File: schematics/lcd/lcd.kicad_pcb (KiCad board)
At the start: 2 copper layers, 68.7 x 45.2 mm, 22 parts, among them J1 Conn_01x07_Socket, U1 NHD-C12832A1Z, U2 TLV70033_SOT23-5, U3 TXS0104EDR

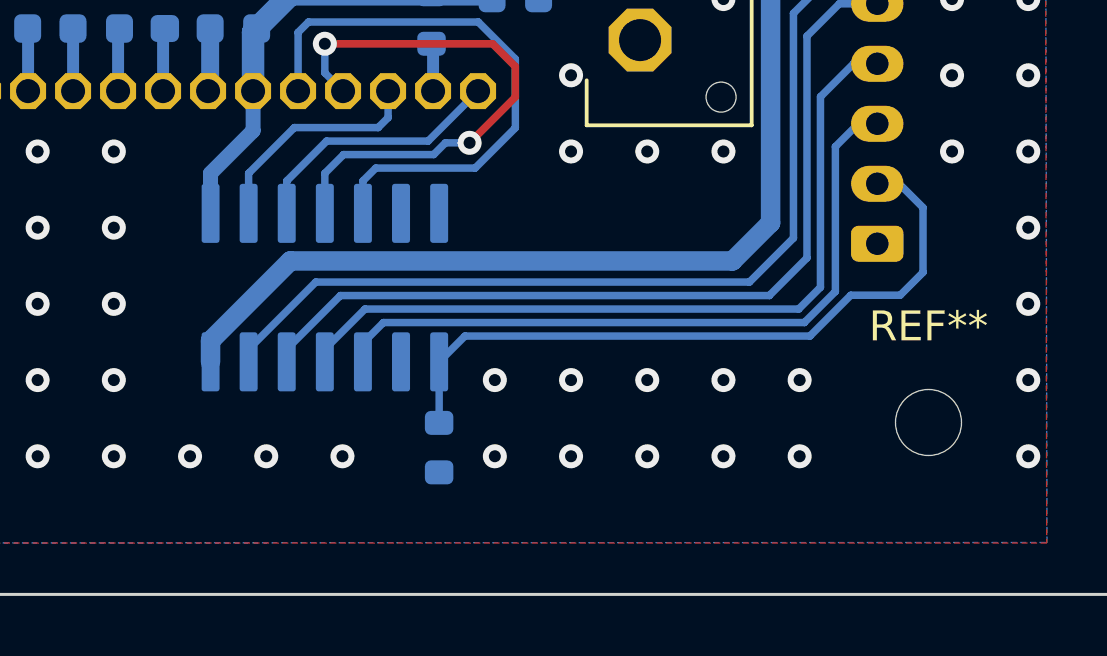
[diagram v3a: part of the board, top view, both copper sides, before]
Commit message: SCH: LCD => removed MB OE connection, now pulled to 3.3, always ON
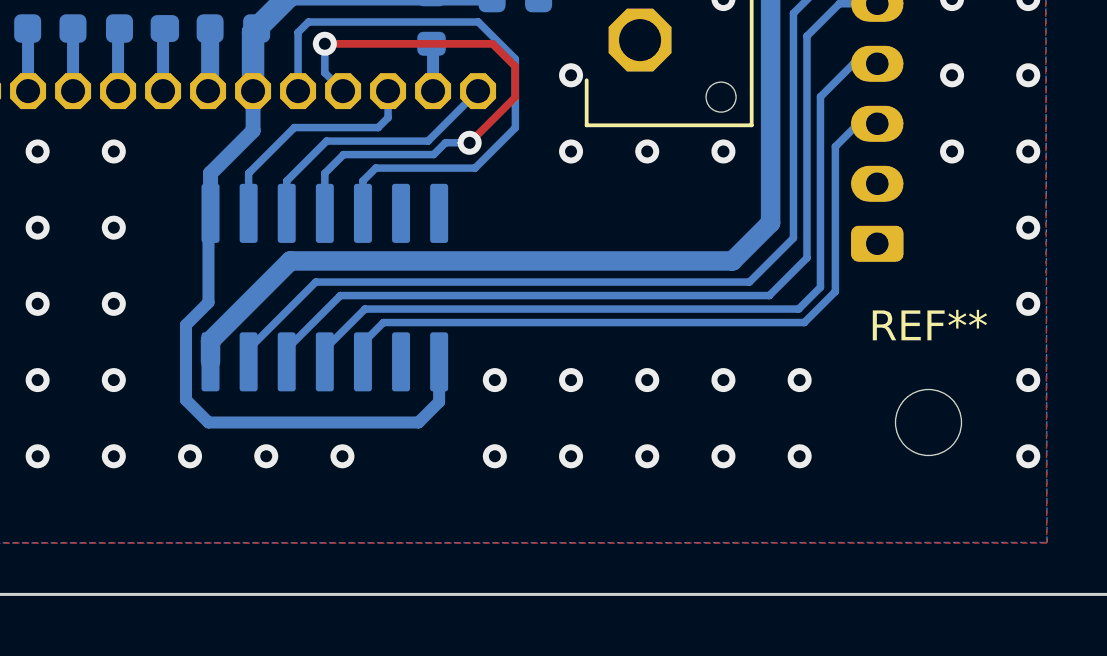
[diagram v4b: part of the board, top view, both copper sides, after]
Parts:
- removed R2: 10K, Resistor_SMD:R_0603_1608Metric
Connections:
- J1 pad 2: /MCU_OE -> GND
- U3 pad 8: /MCU_OE -> +3.3V
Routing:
- net /MCU_OE: track 23.4 -> 0.00 mm
- net +3.3V: track 45.8 -> 62.7 mm
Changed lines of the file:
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@@
   (net 23 "unconnected-(U2-NC-Pad4)")
   (net 24 "VD")
-  (net 25 "/MCU_OE")
   (footprint "MountingHole:MountingHole_2.2mm_M2" (layer "F.Cu")
     (at 67 100)
@@
   (footprint "library:SOIC127P600X175-14N" (layer "B.Cu")
     (at 103.378 95.504 -90)
+    (property "LCSC" "C79342")
     (property "Sheetfile" "lcd.kicad_sch")
     (property "Sheetname" "")
@@
         (effects (font (size 1 1) (thickness 0.15)) (justify mirror))
     )
-    (fp_text value "TXS0104EDR" (at 5.496 2.378) (layer "B.Fab")
+    (fp_text value "TXS0104EDR" (at 8.465 -5.435 90) (layer "B.Fab")
         (effects (font (size 1 1) (thickness 0.15)) (justify mirror))
     )
@@
       (net 2 "GND") (pinfunction "GND") (pintype "power_in"))
     (pad "8" smd roundrect (at 2.475 -3.81 270) (size 1.97 0.6) (layers "B.Cu" "B.Paste" "B.Mask") (roundrect_rratio 0.15)
-      (net 25 "/MCU_OE") (pinfunction "OE") (pintype "input"))
+      (net 3 "+3.3V") (pinfunction "OE") (pintype "input"))
     (pad "9" smd roundrect (at 2.475 -2.54 270) (size 1.97 0.6) (layers "B.Cu" "B.Paste" "B.Mask") (roundrect_rratio 0.15))
     (pad "10" smd roundrect (at 2.475 -1.27 270) (size 1.97 0.6) (layers "B.Cu" "B.Paste" "B.Mask") (roundrect_rratio 0.15)
@@
     )
   )
-  (footprint "Resistor_SMD:R_0603_1608Metric" (layer "B.Cu")
-    (at 107.188 100.838 90)
-    (descr "Resistor SMD 0603 (1608 Metric), square (rectangular) end terminal, IPC_7351 nominal, (Body size source: IPC-SM-782 page 72, https://www.pcb-3d.com/wordpress/wp-content/uploads/ipc-sm-782a_amendment_1_and_2.pdf), generated with kicad-footprint-generator")
-    (tags "resistor")
-    (property "Sheetfile" "lcd.kicad_sch")
-    (property "Sheetname" "")
-    (property "ki_description" "Resistor")
-    (property "ki_keywords" "R res resistor")
-    (property "lcsc" "C25804")
-    (attr smd)
-    (fp_text reference "R2" (at 0 1.43 90) (layer "B.SilkS")
-        (effects (font (size 1 1) (thickness 0.15)) (justify mirror))
-    )
-    (fp_text value "10K" (at 0 -1.43 90) (layer "B.Fab") hide
-        (effects (font (size 1 1) (thickness 0.15)) (justify mirror))
-    )
-    (fp_text user "${REFERENCE}" (at 0 0 90) (layer "B.Fab")
-        (effects (font (size 0.4 0.4) (thickness 0.06)) (justify mirror))
-    )
-    (fp_line (start -0.237258 -0.5225) (end 0.237258 -0.5225)
-      (stroke (width 0.12) (type solid)) (layer "B.SilkS"))
-    (fp_line (start -0.237258 0.5225) (end 0.237258 0.5225)
-      (stroke (width 0.12) (type solid)) (layer "B.SilkS"))
-    (fp_line (start -1.48 -0.73) (end -1.48 0.73)
-      (stroke (width 0.05) (type solid)) (layer "B.CrtYd"))
-    (fp_line (start -1.48 0.73) (end 1.48 0.73)
-      (stroke (width 0.05) (type solid)) (layer "B.CrtYd"))
-    (fp_line (start 1.48 -0.73) (end -1.48 -0.73)
-      (stroke (width 0.05) (type solid)) (layer "B.CrtYd"))
-    (fp_line (start 1.48 0.73) (end 1.48 -0.73)
-      (stroke (width 0.05) (type solid)) (layer "B.CrtYd"))
-    (fp_line (start -0.8 -0.4125) (end -0.8 0.4125)
-      (stroke (width 0.1) (type solid)) (layer "B.Fab"))
-    (fp_line (start -0.8 0.4125) (end 0.8 0.4125)
-      (stroke (width 0.1) (type solid)) (layer "B.Fab"))
-    (fp_line (start 0.8 -0.4125) (end -0.8 -0.4125)
-      (stroke (width 0.1) (type solid)) (layer "B.Fab"))
-    (fp_line (start 0.8 0.4125) (end 0.8 -0.4125)
-      (stroke (width 0.1) (type solid)) (layer "B.Fab"))
-    (pad "1" smd roundrect (at -0.825 0 90) (size 0.8 0.95) (layers "B.Cu" "B.Paste" "B.Mask") (roundrect_rratio 0.25)
-      (net 2 "GND") (pintype "passive"))
-    (pad "2" smd roundrect (at 0.825 0 90) (size 0.8 0.95) (layers "B.Cu" "B.Paste" "B.Mask") (roundrect_rratio 0.25)
-      (net 25 "/MCU_OE") (pintype "passive"))
-    (model "${KICAD6_3DMODEL_DIR}/Resistor_SMD.3dshapes/R_0603_1608Metric.wrl"
-      (offset (xyz 0 0 0))
-      (scale (xyz 1 1 1))
-      (rotate (xyz 0 0 0))
-    )
-  )
   (footprint "Capacitor_SMD:C_0603_1608Metric" (layer "B.Cu")
     (at 98.044 86.093 -90)
@@
       (net 2 "GND") (pinfunction "Pin_1") (pintype "passive"))
     (pad "2" thru_hole oval (at 2 0 90) (size 1.2 1.75) (drill 0.75) (layers "*.Cu" "*.Mask")
-      (net 25 "/MCU_OE") (pinfunction "Pin_2") (pintype "passive"))
+      (net 2 "GND") (pinfunction "Pin_2") (pintype "passive"))
     (pad "3" thru_hole oval (at 4 0 90) (size 1.2 1.75) (drill 0.75) (layers "*.Cu" "*.Mask")
       (net 11 "/MCU_SDA") (pinfunction "Pin_3") (pintype "passive"))
@@
   (segment (start 108.827 85.726) (end 108.953 85.852) (width 0.75) (layer "B.Cu") (net 3))
   (segment (start 101.105 86.868) (end 102.247 85.726) (width 0.75) (layer "B.Cu") (net 3))
+  (segment (start 99.5 93.097) (end 99.568 93.029) (width 0.4) (layer "B.Cu") (net 3))
+  (segment (start 107.188 99.312) (end 106.5 100) (width 0.4) (layer "B.Cu") (net 3))
+  (segment (start 98.75 99.25) (end 98.75 96.749517) (width 0.4) (layer "B.Cu") (net 3))
   (segment (start 99.568 93.029) (end 99.568 91.694) (width 0.5) (layer "B.Cu") (net 3))
+  (segment (start 99.5 100) (end 98.75 99.25) (width 0.4) (layer "B.Cu") (net 3))
+  (segment (start 107.188 97.979) (end 107.188 99.312) (width 0.4) (layer "B.Cu") (net 3))
   (segment (start 100.986 88.954) (end 100.986 86.987) (width 0.75) (layer "B.Cu") (net 3))
   (segment (start 108.712 80.142) (end 105.278 76.708) (width 0.75) (layer "B.Cu") (net 3))
   (segment (start 99.568 91.694) (end 100.986 90.276) (width 0.5) (layer "B.Cu") (net 3))
+  (segment (start 98.75 96.749517) (end 99.5 95.999517) (width 0.4) (layer "B.Cu") (net 3))
   (segment (start 106.934 81.92) (end 106.934 85.726) (width 0.75) (layer "B.Cu") (net 3))
   (segment (start 105.278 76.708) (end 85.808 76.708) (width 0.75) (layer "B.Cu") (net 3))
@@
   (segment (start 100.986 90.276) (end 100.986 88.954) (width 0.5) (layer "B.Cu") (net 3))
   (segment (start 106.934 85.726) (end 108.827 85.726) (width 0.75) (layer "B.Cu") (net 3))
+  (segment (start 99.5 95.999517) (end 99.5 93.097) (width 0.4) (layer "B.Cu") (net 3))
+  (segment (start 106.5 100) (end 99.5 100) (width 0.4) (layer "B.Cu") (net 3))
   (segment (start 102.247 85.726) (end 106.934 85.726) (width 0.75) (layer "B.Cu") (net 3))
   (segment (start 105.486 89.84) (end 105.486 88.954) (width 0.25) (layer "B.Cu") (net 4))
@@
   (segment (start 80.308 75.558) (end 77.978 77.888) (width 1) (layer "B.Cu") (net 24))
   (segment (start 79.286 85.763) (end 79.286 87.254) (width 1) (layer "B.Cu") (net 24))
-  (segment (start 122.522 92.042) (end 121.793 92.042) (width 0.25) (layer "B.Cu") (net 25))
-  (segment (start 119.548188 97.119) (end 120.909188 95.758) (width 0.25) (layer "B.Cu") (net 25))
-  (segment (start 120.909188 95.758) (end 122.555 95.758) (width 0.25) (layer "B.Cu") (net 25))
-  (segment (start 122.555 95.758) (end 123.317 94.996) (width 0.25) (layer "B.Cu") (net 25))
-  (segment (start 107.188 97.979) (end 108.048 97.119) (width 0.25) (layer "B.Cu") (net 25))
-  (segment (start 123.317 92.837) (end 122.522 92.042) (width 0.25) (layer "B.Cu") (net 25))
-  (segment (start 107.188 97.979) (end 107.188 100.013) (width 0.25) (layer "B.Cu") (net 25))
-  (segment (start 108.048 97.119) (end 119.548188 97.119) (width 0.25) (layer "B.Cu") (net 25))
-  (segment (start 123.317 94.996) (end 123.317 92.837) (width 0.25) (layer "B.Cu") (net 25))
   (zone (net 2) (net_name "GND") (layer "F.Cu") (hatch edge 0.5)
     (connect_pads (clearance 0.5))
